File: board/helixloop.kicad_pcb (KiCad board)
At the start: 2 copper layers, 137.5 x 137.5 mm, 372 parts, among them J1 Conn_01x04, J2 Conn_01x02

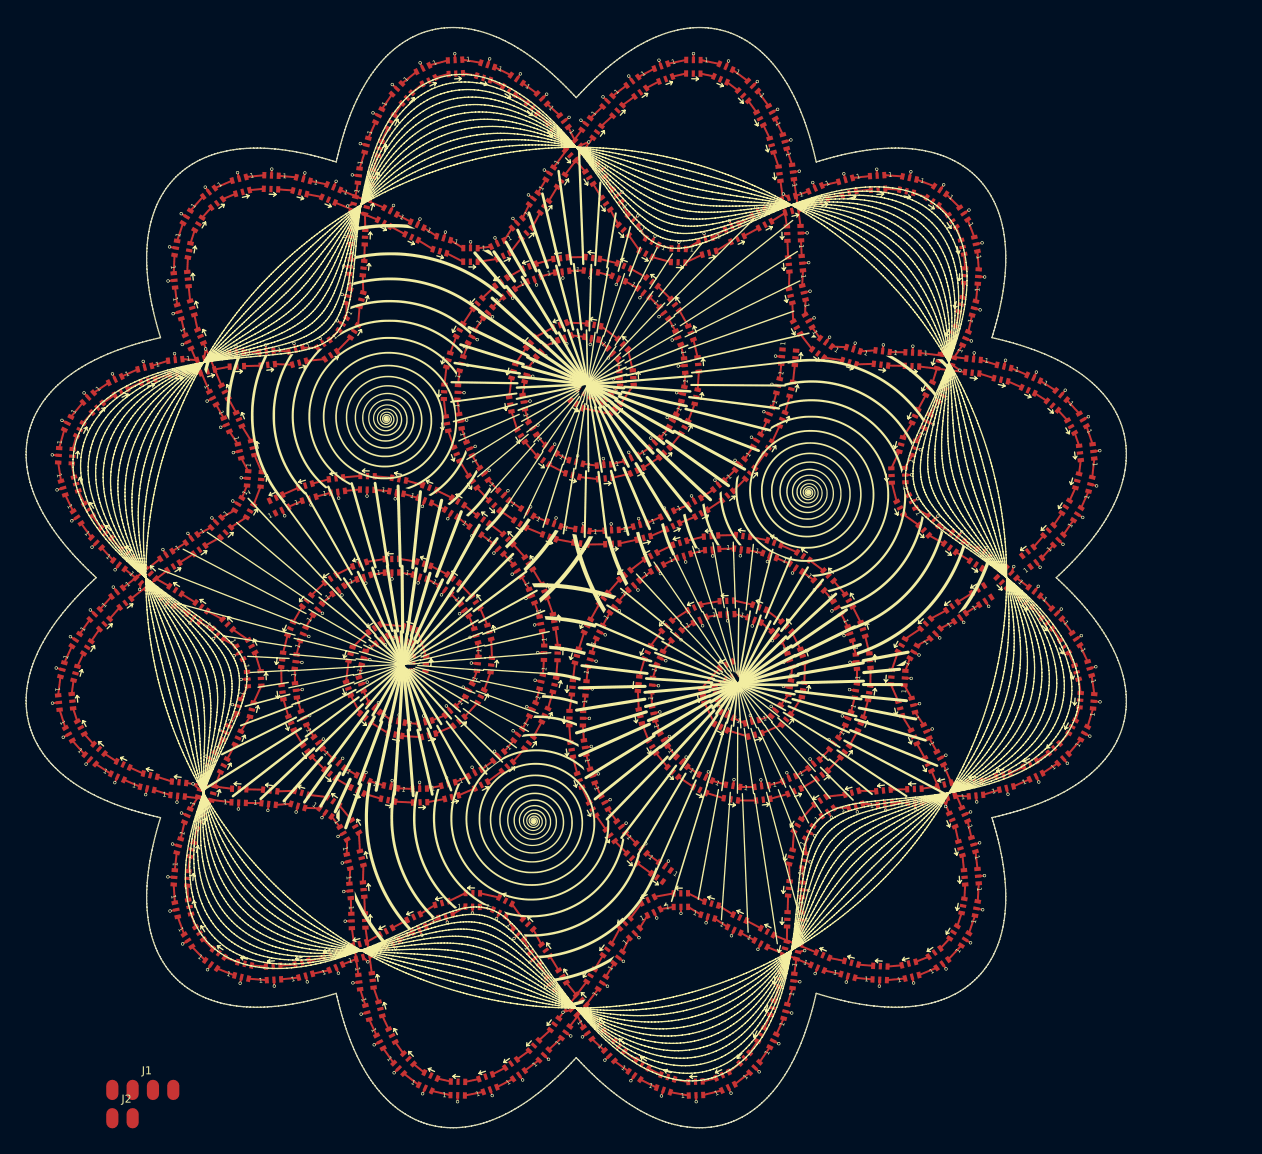
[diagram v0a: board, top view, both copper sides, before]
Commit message: refine the edge.cuts to be nice and smooth
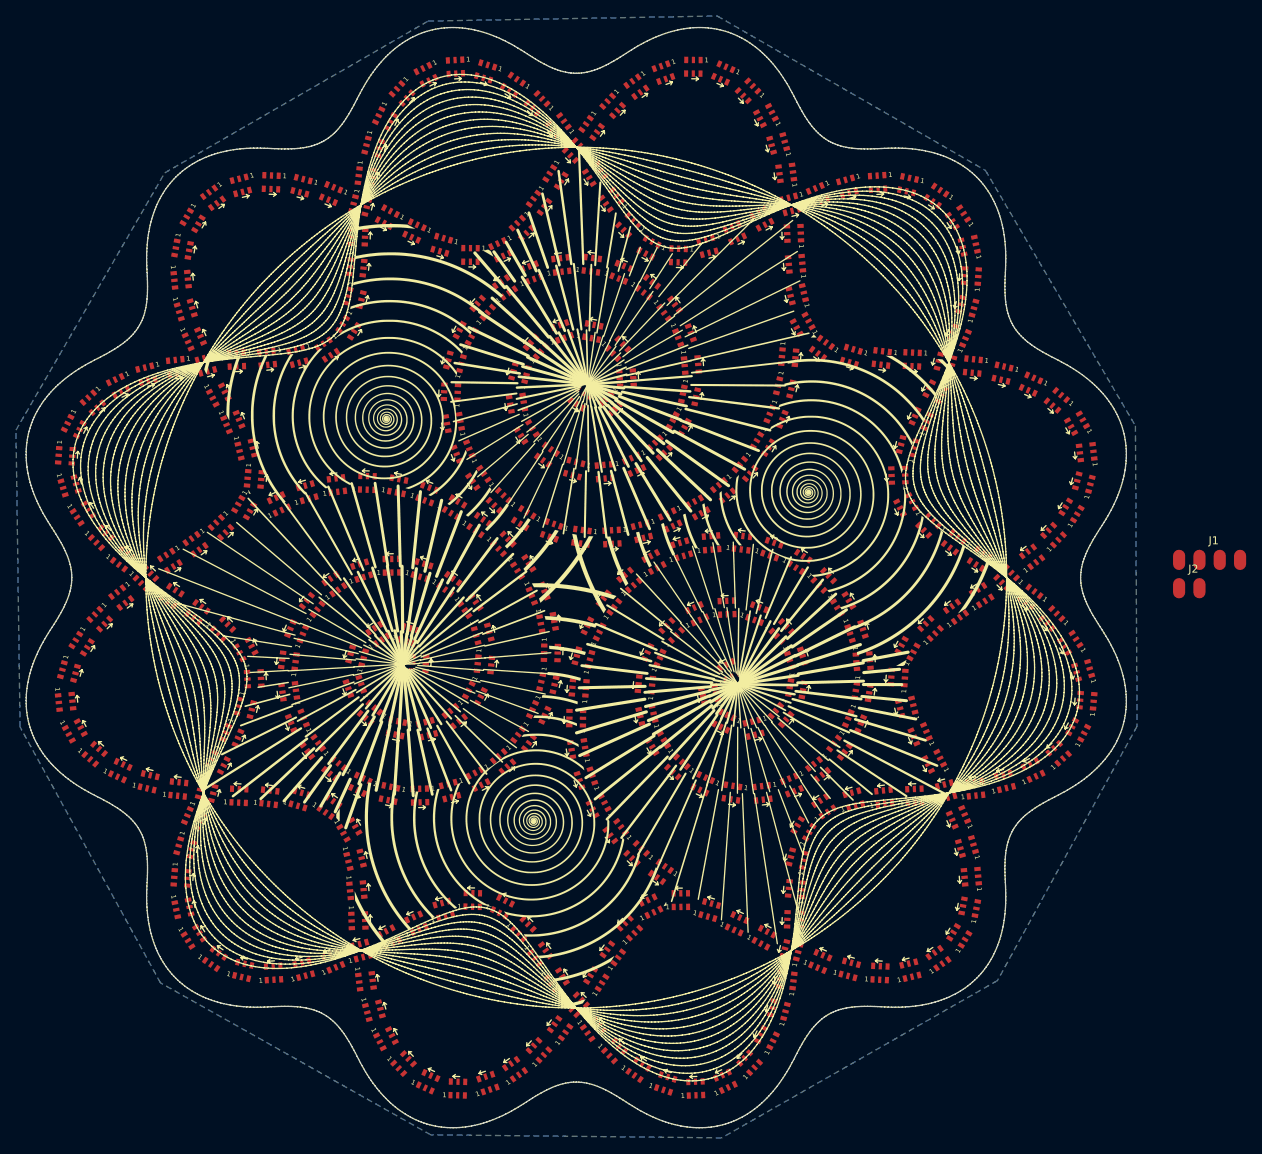
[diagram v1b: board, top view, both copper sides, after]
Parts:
- D1, D10, D100, D101, D102, D103, D104, D105, D106, D107, D108, D109, D11, D110, D111, D112, D113, D114, D115, D116, D117, D118, D119, D12, D120, D121, D122, D123, D124, D125, D126, D127, D128, D129, D13, D130, D131, D132, D133, D134, D135, D136, D137, D138, D139, D14, D140, D141, D142, D143, D144, D145, D146, D147, D148, D149, D15, D150, D151, D152, D153, D154, D155, D156, D157, D158, D159, D16, D160, D161, D162, D163, D164, D165, D166, D167, D168, D169, D17, D170, D171, D172, D173, D174, D175, D176, D177, D178, D179, D18, D180, D181, D182, D183, D184, D185, D186, D187, D188, D189, D19, D190, D191, D192, D193, D194, D195, D196, D197, D198, D199, D2, D20, D200, D201, D202, D203, D204, D205, D206, D207, D208, D209, D21, D210, D211, D212, D213, D214, D215, D216, D217, D218, D219, D22, D220, D221, D222, D223, D224, D225, D226, D227, D228, D229, D23, D230, D231, D232, D233, D234, D235, D236, D237, D238, D239, D24, D240, D241, D242, D243, D244, D245, D246, D247, D248, D249, D25, D250, D251, D252, D253, D254, D255, D256, D257, D258, D259, D26, D260, D261, D262, D263, D264, D265, D266, D267, D268, D269, D27, D270, D271, D272, D273, D274, D275, D276, D277, D278, D279, D28, D280, D281, D282, D283, D284, D285, D286, D287, D288, D289, D29, D290, D291, D292, D293, D294, D295, D296, D297, D298, D299, D3, D30, D300, D301, D302, D303, D304, D305, D306, D307, D308, D309, D31, D310, D311, D312, D313, D314, D315, D316, D317, D318, D319, D32, D320, D321, D322, D323, D324, D325, D326, D327, D328, D329, D33, D330, D331, D332, D333, D334, D335, D336, D337, D338, D339, D34, D340, D341, D342, D343, D344, D345, D346, D347, D348, D349, D35, D350, D351, D352, D353, D354, D355, D356, D357, D358, D359, D36, D360, D361, D362, D363, D364, D365, D366, D367, D368, D369, D37, D38, D39, D4, D40, D41, D42, D43, D44, D45, D46, D47, D48, D49, D5, D50, D51, D52, D53, D54, D55, D56, D57, D58, D59, D6, D60, D61, D62, D63, D64, D65, D66, D67, D68, D69, D7, D70, D71, D72, D73, D74, D75, D76, D77, D78, D79, D8, D80, D81, D82, D83, D84, D85, D86, D87, D88, D89, D9, D90, D91, D92, D93, D94, D95, D96, D97, D98, D99: value SK9822-EC20 -> LED-SK9822-EC20
- spiraldrawing: moved to F.SilkS
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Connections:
- D1 pad 1: Net-(D1-Pad1) -> (no net)
- D1 pad 2: GND -> (no net)
- D1 pad 3: /LED_SDI1 -> (no net)
- D1 pad 4: /LED_CKI1 -> (no net)
- D1 pad 5: +5V -> (no net)
- D1 pad 6: Net-(D1-Pad6) -> (no net)
- D10 pad 1: Net-(D10-Pad1) -> (no net)
- D10 pad 2: GND -> (no net)
- D10 pad 3: Net-(D10-Pad3) -> (no net)
- D10 pad 4: Net-(D10-Pad4) -> (no net)
- D10 pad 5: +5V -> (no net)
- D10 pad 6: Net-(D10-Pad6) -> (no net)
- D100 pad 1: Net-(D100-Pad1) -> (no net)
- D100 pad 2: GND -> (no net)
- D100 pad 3: Net-(D100-Pad3) -> (no net)
- D100 pad 4: Net-(D100-Pad4) -> (no net)
- D100 pad 5: +5V -> (no net)
- D100 pad 6: Net-(D100-Pad6) -> (no net)
- D101 pad 1: Net-(D101-Pad1) -> (no net)
- D101 pad 2: GND -> (no net)
- D101 pad 3: Net-(D100-Pad1) -> (no net)
- D101 pad 4: Net-(D100-Pad6) -> (no net)
- D101 pad 5: +5V -> (no net)
- D101 pad 6: Net-(D101-Pad6) -> (no net)
- D102 pad 1: Net-(D102-Pad1) -> (no net)
- D102 pad 2: GND -> (no net)
- D102 pad 3: Net-(D101-Pad1) -> (no net)
- D102 pad 4: Net-(D101-Pad6) -> (no net)
- D102 pad 5: +5V -> (no net)
- D102 pad 6: Net-(D102-Pad6) -> (no net)
- D103 pad 1: Net-(D103-Pad1) -> (no net)
- D103 pad 2: GND -> (no net)
- D103 pad 3: Net-(D102-Pad1) -> (no net)
- D103 pad 4: Net-(D102-Pad6) -> (no net)
- D103 pad 5: +5V -> (no net)
- D103 pad 6: Net-(D103-Pad6) -> (no net)
- D104 pad 1: Net-(D104-Pad1) -> (no net)
- D104 pad 2: GND -> (no net)
- D104 pad 3: Net-(D103-Pad1) -> (no net)
- D104 pad 4: Net-(D103-Pad6) -> (no net)
- D104 pad 5: +5V -> (no net)
- D104 pad 6: Net-(D104-Pad6) -> (no net)
- D105 pad 1: Net-(D105-Pad1) -> (no net)
- D105 pad 2: GND -> (no net)
- D105 pad 3: Net-(D104-Pad1) -> (no net)
- D105 pad 4: Net-(D104-Pad6) -> (no net)
- D105 pad 5: +5V -> (no net)
- D105 pad 6: Net-(D105-Pad6) -> (no net)
- D106 pad 1: Net-(D106-Pad1) -> (no net)
- D106 pad 2: GND -> (no net)
- D106 pad 3: Net-(D105-Pad1) -> (no net)
- D106 pad 4: Net-(D105-Pad6) -> (no net)
- D106 pad 5: +5V -> (no net)
- D106 pad 6: Net-(D106-Pad6) -> (no net)
- D107 pad 1: Net-(D107-Pad1) -> (no net)
- D107 pad 2: GND -> (no net)
- D107 pad 3: Net-(D106-Pad1) -> (no net)
- D107 pad 4: Net-(D106-Pad6) -> (no net)
- D107 pad 5: +5V -> (no net)
- D107 pad 6: Net-(D107-Pad6) -> (no net)
- D108 pad 1: Net-(D108-Pad1) -> (no net)
- D108 pad 2: GND -> (no net)
- D108 pad 3: Net-(D107-Pad1) -> (no net)
- D108 pad 4: Net-(D107-Pad6) -> (no net)
- D108 pad 5: +5V -> (no net)
- D108 pad 6: Net-(D108-Pad6) -> (no net)
- D109 pad 1: Net-(D109-Pad1) -> (no net)
- D109 pad 2: GND -> (no net)
- D109 pad 3: Net-(D108-Pad1) -> (no net)
- D109 pad 4: Net-(D108-Pad6) -> (no net)
- D109 pad 5: +5V -> (no net)
- D109 pad 6: Net-(D109-Pad6) -> (no net)
- D11 pad 1: Net-(D11-Pad1) -> (no net)
- D11 pad 2: GND -> (no net)
- D11 pad 3: Net-(D10-Pad1) -> (no net)
- D11 pad 4: Net-(D10-Pad6) -> (no net)
- D11 pad 5: +5V -> (no net)
- D11 pad 6: Net-(D11-Pad6) -> (no net)
- D110 pad 1: Net-(D110-Pad1) -> (no net)
- D110 pad 2: GND -> (no net)
- D110 pad 3: Net-(D109-Pad1) -> (no net)
- D110 pad 4: Net-(D109-Pad6) -> (no net)
- D110 pad 5: +5V -> (no net)
- D110 pad 6: Net-(D110-Pad6) -> (no net)
- D111 pad 1: Net-(D111-Pad1) -> (no net)
- D111 pad 2: GND -> (no net)
- D111 pad 3: Net-(D110-Pad1) -> (no net)
- D111 pad 4: Net-(D110-Pad6) -> (no net)
- D111 pad 5: +5V -> (no net)
- D111 pad 6: Net-(D111-Pad6) -> (no net)
- D112 pad 1: Net-(D112-Pad1) -> (no net)
- D112 pad 2: GND -> (no net)
- D112 pad 3: Net-(D111-Pad1) -> (no net)
- D112 pad 4: Net-(D111-Pad6) -> (no net)
- D112 pad 5: +5V -> (no net)
- D112 pad 6: Net-(D112-Pad6) -> (no net)
- D113 pad 1: Net-(D113-Pad1) -> (no net)
- D113 pad 2: GND -> (no net)
- D113 pad 3: Net-(D112-Pad1) -> (no net)
- D113 pad 4: Net-(D112-Pad6) -> (no net)
- D113 pad 5: +5V -> (no net)
- D113 pad 6: Net-(D113-Pad6) -> (no net)
- D114 pad 1: Net-(D114-Pad1) -> (no net)
- D114 pad 2: GND -> (no net)
- D114 pad 3: Net-(D113-Pad1) -> (no net)
- D114 pad 4: Net-(D113-Pad6) -> (no net)
- D114 pad 5: +5V -> (no net)
- D114 pad 6: Net-(D114-Pad6) -> (no net)
- D115 pad 1: Net-(D115-Pad1) -> (no net)
- D115 pad 2: GND -> (no net)
- D115 pad 3: Net-(D114-Pad1) -> (no net)
- D115 pad 4: Net-(D114-Pad6) -> (no net)
- D115 pad 5: +5V -> (no net)
- D115 pad 6: Net-(D115-Pad6) -> (no net)
- D116 pad 1: Net-(D116-Pad1) -> (no net)
- D116 pad 2: GND -> (no net)
- D116 pad 3: Net-(D115-Pad1) -> (no net)
- D116 pad 4: Net-(D115-Pad6) -> (no net)
- D116 pad 5: +5V -> (no net)
- D116 pad 6: Net-(D116-Pad6) -> (no net)
- D117 pad 1: Net-(D117-Pad1) -> (no net)
- D117 pad 2: GND -> (no net)
- D117 pad 3: Net-(D116-Pad1) -> (no net)
- D117 pad 4: Net-(D116-Pad6) -> (no net)
- D117 pad 5: +5V -> (no net)
- D117 pad 6: Net-(D117-Pad6) -> (no net)
- D118 pad 1: Net-(D118-Pad1) -> (no net)
- D118 pad 2: GND -> (no net)
- D118 pad 3: Net-(D117-Pad1) -> (no net)
- D118 pad 4: Net-(D117-Pad6) -> (no net)
- D118 pad 5: +5V -> (no net)
- D118 pad 6: Net-(D118-Pad6) -> (no net)
- D119 pad 1: Net-(D119-Pad1) -> (no net)
- D119 pad 2: GND -> (no net)
- D119 pad 3: Net-(D118-Pad1) -> (no net)
- D119 pad 4: Net-(D118-Pad6) -> (no net)
- D119 pad 5: +5V -> (no net)
- D119 pad 6: Net-(D119-Pad6) -> (no net)
- D12 pad 1: Net-(D12-Pad1) -> (no net)
- D12 pad 2: GND -> (no net)
- D12 pad 3: Net-(D11-Pad1) -> (no net)
- D12 pad 4: Net-(D11-Pad6) -> (no net)
- D12 pad 5: +5V -> (no net)
- D12 pad 6: Net-(D12-Pad6) -> (no net)
- D120 pad 1: Net-(D120-Pad1) -> (no net)
- D120 pad 2: GND -> (no net)
- D120 pad 3: Net-(D119-Pad1) -> (no net)
- D120 pad 4: Net-(D119-Pad6) -> (no net)
- D120 pad 5: +5V -> (no net)
- D120 pad 6: Net-(D120-Pad6) -> (no net)
- D121 pad 1: Net-(D121-Pad1) -> (no net)
- D121 pad 2: GND -> (no net)
- D121 pad 3: Net-(D120-Pad1) -> (no net)
- D121 pad 4: Net-(D120-Pad6) -> (no net)
- D121 pad 5: +5V -> (no net)
- D121 pad 6: Net-(D121-Pad6) -> (no net)
- D122 pad 1: Net-(D122-Pad1) -> (no net)
- D122 pad 2: GND -> (no net)
- D122 pad 3: Net-(D121-Pad1) -> (no net)
- D122 pad 4: Net-(D121-Pad6) -> (no net)
- D122 pad 5: +5V -> (no net)
- D122 pad 6: Net-(D122-Pad6) -> (no net)
- D123 pad 1: /SK9822 LED Array 1/LED_SDO -> (no net)
- D123 pad 2: GND -> (no net)
- D123 pad 3: Net-(D122-Pad1) -> (no net)
- D123 pad 4: Net-(D122-Pad6) -> (no net)
- D123 pad 5: +5V -> (no net)
- D123 pad 6: /SK9822 LED Array 1/LED_CKO -> (no net)
- D124 pad 1: Net-(D124-Pad1) -> (no net)
- D124 pad 2: GND -> (no net)
- D124 pad 3: /SK9822 LED Array 1/LED_SDO -> (no net)
- D124 pad 4: /SK9822 LED Array 1/LED_CKO -> (no net)
- D124 pad 5: +5V -> (no net)
- D124 pad 6: Net-(D124-Pad6) -> (no net)
- D125 pad 1: Net-(D125-Pad1) -> (no net)
- D125 pad 2: GND -> (no net)
- D125 pad 3: Net-(D124-Pad1) -> (no net)
- D125 pad 4: Net-(D124-Pad6) -> (no net)
- D125 pad 5: +5V -> (no net)
- D125 pad 6: Net-(D125-Pad6) -> (no net)
- D126 pad 1: Net-(D126-Pad1) -> (no net)
- D126 pad 2: GND -> (no net)
- D126 pad 3: Net-(D125-Pad1) -> (no net)
- D126 pad 4: Net-(D125-Pad6) -> (no net)
- D126 pad 5: +5V -> (no net)
- D126 pad 6: Net-(D126-Pad6) -> (no net)
- D127 pad 1: Net-(D127-Pad1) -> (no net)
- D127 pad 2: GND -> (no net)
- D127 pad 3: Net-(D126-Pad1) -> (no net)
- D127 pad 4: Net-(D126-Pad6) -> (no net)
- D127 pad 5: +5V -> (no net)
- D127 pad 6: Net-(D127-Pad6) -> (no net)
- D128 pad 1: Net-(D128-Pad1) -> (no net)
- D128 pad 2: GND -> (no net)
- D128 pad 3: Net-(D127-Pad1) -> (no net)
- D128 pad 4: Net-(D127-Pad6) -> (no net)
- D128 pad 5: +5V -> (no net)
- D128 pad 6: Net-(D128-Pad6) -> (no net)
- D129 pad 1: Net-(D129-Pad1) -> (no net)
- D129 pad 2: GND -> (no net)
- D129 pad 3: Net-(D128-Pad1) -> (no net)
- D129 pad 4: Net-(D128-Pad6) -> (no net)
- D129 pad 5: +5V -> (no net)
- D129 pad 6: Net-(D129-Pad6) -> (no net)
- D13 pad 1: Net-(D13-Pad1) -> (no net)
- D13 pad 2: GND -> (no net)
- D13 pad 3: Net-(D12-Pad1) -> (no net)
- D13 pad 4: Net-(D12-Pad6) -> (no net)
- D13 pad 5: +5V -> (no net)
- D13 pad 6: Net-(D13-Pad6) -> (no net)
- D130 pad 1: Net-(D130-Pad1) -> (no net)
- D130 pad 2: GND -> (no net)
- D130 pad 3: Net-(D129-Pad1) -> (no net)
- D130 pad 4: Net-(D129-Pad6) -> (no net)
- D130 pad 5: +5V -> (no net)
- D130 pad 6: Net-(D130-Pad6) -> (no net)
- D131 pad 1: Net-(D131-Pad1) -> (no net)
- D131 pad 2: GND -> (no net)
- D131 pad 3: Net-(D130-Pad1) -> (no net)
- D131 pad 4: Net-(D130-Pad6) -> (no net)
- D131 pad 5: +5V -> (no net)
- D131 pad 6: Net-(D131-Pad6) -> (no net)
- D132 pad 1: Net-(D132-Pad1) -> (no net)
- D132 pad 2: GND -> (no net)
- D132 pad 3: Net-(D131-Pad1) -> (no net)
- D132 pad 4: Net-(D131-Pad6) -> (no net)
- D132 pad 5: +5V -> (no net)
- D132 pad 6: Net-(D132-Pad6) -> (no net)
- D133 pad 1: Net-(D133-Pad1) -> (no net)
- D133 pad 2: GND -> (no net)
- D133 pad 3: Net-(D132-Pad1) -> (no net)
- D133 pad 4: Net-(D132-Pad6) -> (no net)
- D133 pad 5: +5V -> (no net)
- D133 pad 6: Net-(D133-Pad6) -> (no net)
- D134 pad 1: Net-(D134-Pad1) -> (no net)
- D134 pad 2: GND -> (no net)
- D134 pad 3: Net-(D133-Pad1) -> (no net)
- D134 pad 4: Net-(D133-Pad6) -> (no net)
- D134 pad 5: +5V -> (no net)
- D134 pad 6: Net-(D134-Pad6) -> (no net)
- D135 pad 1: Net-(D135-Pad1) -> (no net)
- D135 pad 2: GND -> (no net)
- D135 pad 3: Net-(D134-Pad1) -> (no net)
- D135 pad 4: Net-(D134-Pad6) -> (no net)
- D135 pad 5: +5V -> (no net)
- D135 pad 6: Net-(D135-Pad6) -> (no net)
- D136 pad 1: Net-(D136-Pad1) -> (no net)
- D136 pad 2: GND -> (no net)
- D136 pad 3: Net-(D135-Pad1) -> (no net)
- D136 pad 4: Net-(D135-Pad6) -> (no net)
- D136 pad 5: +5V -> (no net)
- D136 pad 6: Net-(D136-Pad6) -> (no net)
- D137 pad 1: Net-(D137-Pad1) -> (no net)
- D137 pad 2: GND -> (no net)
- D137 pad 3: Net-(D136-Pad1) -> (no net)
- D137 pad 4: Net-(D136-Pad6) -> (no net)
- D137 pad 5: +5V -> (no net)
- D137 pad 6: Net-(D137-Pad6) -> (no net)
- D138 pad 1: Net-(D139-Pad3) -> (no net)
- D138 pad 2: GND -> (no net)
- D138 pad 3: Net-(D137-Pad1) -> (no net)
- D138 pad 4: Net-(D137-Pad6) -> (no net)
- D138 pad 5: +5V -> (no net)
- D138 pad 6: Net-(D139-Pad4) -> (no net)
- D139 pad 1: Net-(D139-Pad1) -> (no net)
- D139 pad 2: GND -> (no net)
- D139 pad 3: Net-(D139-Pad3) -> (no net)
- D139 pad 4: Net-(D139-Pad4) -> (no net)
- D139 pad 5: +5V -> (no net)
- D139 pad 6: Net-(D139-Pad6) -> (no net)
- D14 pad 1: Net-(D14-Pad1) -> (no net)
- D14 pad 2: GND -> (no net)
- D14 pad 3: Net-(D13-Pad1) -> (no net)
- D14 pad 4: Net-(D13-Pad6) -> (no net)
- D14 pad 5: +5V -> (no net)
- D14 pad 6: Net-(D14-Pad6) -> (no net)
- D140 pad 1: Net-(D140-Pad1) -> (no net)
- D140 pad 2: GND -> (no net)
- D140 pad 3: Net-(D139-Pad1) -> (no net)
- D140 pad 4: Net-(D139-Pad6) -> (no net)
- D140 pad 5: +5V -> (no net)
- D140 pad 6: Net-(D140-Pad6) -> (no net)
- D141 pad 1: Net-(D141-Pad1) -> (no net)
- D141 pad 2: GND -> (no net)
- D141 pad 3: Net-(D140-Pad1) -> (no net)
- D141 pad 4: Net-(D140-Pad6) -> (no net)
- D141 pad 5: +5V -> (no net)
- D141 pad 6: Net-(D141-Pad6) -> (no net)
- D142 pad 1: Net-(D142-Pad1) -> (no net)
- D142 pad 2: GND -> (no net)
- D142 pad 3: Net-(D141-Pad1) -> (no net)
- D142 pad 4: Net-(D141-Pad6) -> (no net)
- D142 pad 5: +5V -> (no net)
- D142 pad 6: Net-(D142-Pad6) -> (no net)
- D143 pad 1: Net-(D143-Pad1) -> (no net)
- D143 pad 2: GND -> (no net)
- D143 pad 3: Net-(D142-Pad1) -> (no net)
- D143 pad 4: Net-(D142-Pad6) -> (no net)
- D143 pad 5: +5V -> (no net)
- D143 pad 6: Net-(D143-Pad6) -> (no net)
- D144 pad 1: Net-(D144-Pad1) -> (no net)
- D144 pad 2: GND -> (no net)
- D144 pad 3: Net-(D143-Pad1) -> (no net)
- D144 pad 4: Net-(D143-Pad6) -> (no net)
- D144 pad 5: +5V -> (no net)
- D144 pad 6: Net-(D144-Pad6) -> (no net)
- D145 pad 1: Net-(D145-Pad1) -> (no net)
- D145 pad 2: GND -> (no net)
- D145 pad 3: Net-(D144-Pad1) -> (no net)
- D145 pad 4: Net-(D144-Pad6) -> (no net)
- D145 pad 5: +5V -> (no net)
- D145 pad 6: Net-(D145-Pad6) -> (no net)
- D146 pad 1: Net-(D146-Pad1) -> (no net)
- D146 pad 2: GND -> (no net)
- D146 pad 3: Net-(D145-Pad1) -> (no net)
- D146 pad 4: Net-(D145-Pad6) -> (no net)
- D146 pad 5: +5V -> (no net)
- D146 pad 6: Net-(D146-Pad6) -> (no net)
- D147 pad 1: Net-(D147-Pad1) -> (no net)
- D147 pad 2: GND -> (no net)
- D147 pad 3: Net-(D146-Pad1) -> (no net)
- D147 pad 4: Net-(D146-Pad6) -> (no net)
- D147 pad 5: +5V -> (no net)
- D147 pad 6: Net-(D147-Pad6) -> (no net)
- D148 pad 1: Net-(D148-Pad1) -> (no net)
- D148 pad 2: GND -> (no net)
- D148 pad 3: Net-(D147-Pad1) -> (no net)
- D148 pad 4: Net-(D147-Pad6) -> (no net)
- D148 pad 5: +5V -> (no net)
- D148 pad 6: Net-(D148-Pad6) -> (no net)
- D149 pad 1: Net-(D149-Pad1) -> (no net)
- D149 pad 2: GND -> (no net)
- D149 pad 3: Net-(D148-Pad1) -> (no net)
- D149 pad 4: Net-(D148-Pad6) -> (no net)
- D149 pad 5: +5V -> (no net)
- D149 pad 6: Net-(D149-Pad6) -> (no net)
- D15 pad 1: Net-(D16-Pad3) -> (no net)
- D15 pad 2: GND -> (no net)
- D15 pad 3: Net-(D14-Pad1) -> (no net)
- D15 pad 4: Net-(D14-Pad6) -> (no net)
- D15 pad 5: +5V -> (no net)
- D15 pad 6: Net-(D16-Pad4) -> (no net)
- D150 pad 1: Net-(D150-Pad1) -> (no net)
- D150 pad 2: GND -> (no net)
- D150 pad 3: Net-(D149-Pad1) -> (no net)
- D150 pad 4: Net-(D149-Pad6) -> (no net)
- D150 pad 5: +5V -> (no net)
- D150 pad 6: Net-(D150-Pad6) -> (no net)
- D151 pad 1: Net-(D151-Pad1) -> (no net)
- D151 pad 2: GND -> (no net)
- D151 pad 3: Net-(D150-Pad1) -> (no net)
- D151 pad 4: Net-(D150-Pad6) -> (no net)
- D151 pad 5: +5V -> (no net)
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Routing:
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- added copper zone on B.Cu, net GND
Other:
- outline, holes or cut-outs redrawn

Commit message: finally get pixels all aligned right by laying out the sine-wave in chunks and using different pixel spacing for outer vs inner curve
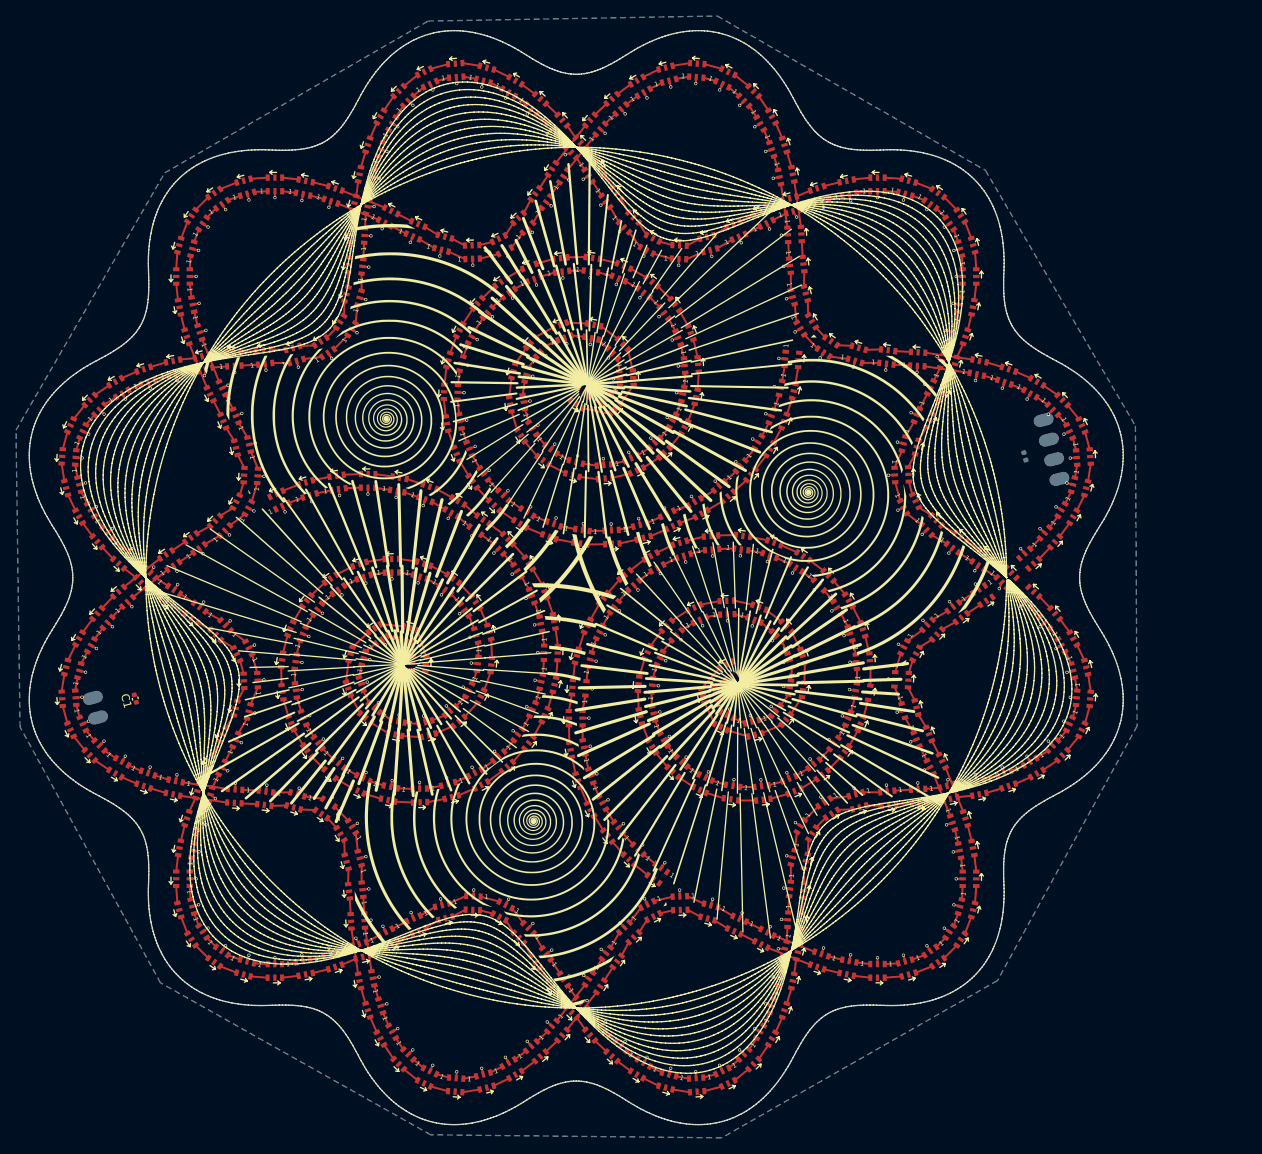
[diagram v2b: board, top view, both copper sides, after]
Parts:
- added C1: 10uF, Capacitor_SMD:C_0402_1005Metric, F.Cu at (44.9, 115.1)
- added C2: 10uF, Capacitor_SMD:C_0402_1005Metric, B.Cu at (156.1, 84.8)
- J1, J2: moved to B.Cu
- spiraldrawing: moved to F.Cu
- moved J2 137.4 mm to (40.0, 116.2), turned to -75 degrees
- moved D148 115.9 mm to (102.4, 43.4), turned to -131.363 degrees
- moved D202 115.8 mm to (97.6, 156.6), turned to 48.6371 degrees
- moved D147 115.7 mm to (105.0, 40.8), turned to -138.828 degrees
- moved D201 115.6 mm to (95.0, 159.2), turned to 41.1715 degrees
- moved D91 113.3 mm to (102.4, 156.6), turned to -48.6561 degrees
- moved D31 113.1 mm to (97.6, 43.4), turned to 131.344 degrees
- moved D90 113.1 mm to (100.0, 153.7), turned to -44.9689 degrees
- moved D30 113.0 mm to (100.0, 46.3), turned to 135.031 degrees
- moved D92 112.7 mm to (105.0, 159.2), turned to -41.201 degrees
- moved D32 112.7 mm to (95.0, 40.8), turned to 138.799 degrees
- moved D89 112.5 mm to (97.7, 150.7), turned to -56.7109 degrees
- moved D29 112.4 mm to (102.3, 49.3), turned to 123.289 degrees
- moved D149 112.2 mm to (97.7, 49.4), turned to -123.328 degrees
- moved D203 112.1 mm to (102.3, 150.6), turned to 56.6721 degrees
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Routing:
- net (no net): track 0.00 -> 1552.5 mm, vias 0 -> 14
- net GND: track 0.00 -> 282.4 mm, vias 0 -> 353
- net +5V: track 0.00 -> 1.60 mm, vias 0 -> 2
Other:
- board size 137.5 x 137.5 mm -> 136.7 x 136.7 mm

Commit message: draft routing
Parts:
- C1: moved to B.Cu
- D1, D10, D100, D101, D102, D103, D104, D105, D106, D107, D108, D109, D11, D110, D111, D112, D113, D114, D115, D116, D117, D118, D119, D12, D120, D121, D122, D123, D124, D125, D126, D127, D128, D129, D13, D130, D131, D132, D133, D134, D135, D136, D137, D138, D139, D14, D140, D141, D142, D143, D144, D145, D146, D147, D148, D149, D15, D150, D151, D152, D153, D154, D155, D156, D157, D158, D159, D16, D160, D161, D162, D163, D164, D165, D166, D167, D168, D169, D17, D170, D171, D172, D173, D174, D175, D176, D177, D178, D179, D18, D180, D181, D182, D183, D184, D185, D186, D187, D188, D189, D19, D190, D191, D192, D193, D194, D195, D196, D197, D198, D199, D2, D20, D200, D201, D202, D203, D204, D205, D206, D207, D208, D209, D21, D210, D211, D212, D213, D214, D215, D216, D217, D218, D219, D22, D220, D221, D222, D223, D224, D225, D226, D227, D228, D229, D23, D230, D231, D232, D233, D234, D235, D236, D237, D238, D239, D24, D240, D241, D242, D243, D244, D245, D246, D247, D248, D249, D25, D250, D251, D252, D253, D254, D255, D256, D257, D258, D259, D26, D260, D261, D262, D263, D264, D265, D266, D267, D268, D269, D27, D270, D271, D272, D273, D274, D275, D276, D277, D278, D279, D28, D280, D281, D282, D283, D284, D285, D286, D287, D288, D289, D29, D290, D291, D292, D293, D294, D295, D296, D297, D298, D299, D3, D30, D300, D301, D302, D303, D304, D305, D306, D307, D308, D309, D31, D310, D311, D312, D313, D314, D315, D316, D317, D318, D319, D32, D320, D321, D322, D323, D324, D325, D326, D327, D328, D329, D33, D330, D331, D332, D333, D334, D335, D336, D337, D338, D339, D34, D340, D341, D342, D343, D344, D345, D346, D347, D348, D349, D35, D350, D351, D352, D353, D354, D355, D356, D357, D358, D359, D36, D360, D361, D362, D363, D364, D365, D366, D367, D368, D369, D37, D38, D39, D4, D40, D41, D42, D43, D44, D45, D46, D47, D48, D49, D5, D50, D51, D52, D53, D54, D55, D56, D57, D58, D59, D6, D60, D61, D62, D63, D64, D65, D66, D67, D68, D69, D7, D70, D71, D72, D73, D74, D75, D76, D77, D78, D79, D8, D80, D81, D82, D83, D84, D85, D86, D87, D88, D89, D9, D90, D91, D92, D93, D94, D95, D96, D97, D98, D99: value LED-SK9822-EC20 -> SK9822-EC20
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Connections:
- D1 pad 1: (no net) -> Net-(D1-Pad1)
- D1 pad 2: (no net) -> GND
- D1 pad 3: (no net) -> /LED_SDI1
- D1 pad 4: (no net) -> /LED_CKI1
- D1 pad 5: (no net) -> +5V
- D1 pad 6: (no net) -> Net-(D1-Pad6)
- D10 pad 1: (no net) -> Net-(D10-Pad1)
- D10 pad 2: (no net) -> GND
- D10 pad 3: (no net) -> Net-(D10-Pad3)
- D10 pad 4: (no net) -> Net-(D10-Pad4)
- D10 pad 5: (no net) -> +5V
- D10 pad 6: (no net) -> Net-(D10-Pad6)
- D100 pad 1: (no net) -> Net-(D100-Pad1)
- D100 pad 2: (no net) -> GND
- D100 pad 3: (no net) -> Net-(D100-Pad3)
- D100 pad 4: (no net) -> Net-(D100-Pad4)
- D100 pad 5: (no net) -> +5V
- D100 pad 6: (no net) -> Net-(D100-Pad6)
- D101 pad 1: (no net) -> Net-(D101-Pad1)
- D101 pad 2: (no net) -> GND
- D101 pad 3: (no net) -> Net-(D100-Pad1)
- D101 pad 4: (no net) -> Net-(D100-Pad6)
- D101 pad 5: (no net) -> +5V
- D101 pad 6: (no net) -> Net-(D101-Pad6)
- D102 pad 1: (no net) -> Net-(D102-Pad1)
- D102 pad 2: (no net) -> GND
- D102 pad 3: (no net) -> Net-(D101-Pad1)
- D102 pad 4: (no net) -> Net-(D101-Pad6)
- D102 pad 5: (no net) -> +5V
- D102 pad 6: (no net) -> Net-(D102-Pad6)
- D103 pad 1: (no net) -> Net-(D103-Pad1)
- D103 pad 2: (no net) -> GND
- D103 pad 3: (no net) -> Net-(D102-Pad1)
- D103 pad 4: (no net) -> Net-(D102-Pad6)
- D103 pad 5: (no net) -> +5V
- D103 pad 6: (no net) -> Net-(D103-Pad6)
- D104 pad 1: (no net) -> Net-(D104-Pad1)
- D104 pad 2: (no net) -> GND
- D104 pad 3: (no net) -> Net-(D103-Pad1)
- D104 pad 4: (no net) -> Net-(D103-Pad6)
- D104 pad 5: (no net) -> +5V
- D104 pad 6: (no net) -> Net-(D104-Pad6)
- D105 pad 1: (no net) -> Net-(D105-Pad1)
- D105 pad 2: (no net) -> GND
- D105 pad 3: (no net) -> Net-(D104-Pad1)
- D105 pad 4: (no net) -> Net-(D104-Pad6)
- D105 pad 5: (no net) -> +5V
- D105 pad 6: (no net) -> Net-(D105-Pad6)
- D106 pad 1: (no net) -> Net-(D106-Pad1)
- D106 pad 2: (no net) -> GND
- D106 pad 3: (no net) -> Net-(D105-Pad1)
- D106 pad 4: (no net) -> Net-(D105-Pad6)
- D106 pad 5: (no net) -> +5V
- D106 pad 6: (no net) -> Net-(D106-Pad6)
- D107 pad 1: (no net) -> Net-(D107-Pad1)
- D107 pad 2: (no net) -> GND
- D107 pad 3: (no net) -> Net-(D106-Pad1)
- D107 pad 4: (no net) -> Net-(D106-Pad6)
- D107 pad 5: (no net) -> +5V
- D107 pad 6: (no net) -> Net-(D107-Pad6)
- D108 pad 1: (no net) -> Net-(D108-Pad1)
- D108 pad 2: (no net) -> GND
- D108 pad 3: (no net) -> Net-(D107-Pad1)
- D108 pad 4: (no net) -> Net-(D107-Pad6)
- D108 pad 5: (no net) -> +5V
- D108 pad 6: (no net) -> Net-(D108-Pad6)
- D109 pad 1: (no net) -> Net-(D109-Pad1)
- D109 pad 2: (no net) -> GND
- D109 pad 3: (no net) -> Net-(D108-Pad1)
- D109 pad 4: (no net) -> Net-(D108-Pad6)
- D109 pad 5: (no net) -> +5V
- D109 pad 6: (no net) -> Net-(D109-Pad6)
- D11 pad 1: (no net) -> Net-(D11-Pad1)
- D11 pad 2: (no net) -> GND
- D11 pad 3: (no net) -> Net-(D10-Pad1)
- D11 pad 4: (no net) -> Net-(D10-Pad6)
- D11 pad 5: (no net) -> +5V
- D11 pad 6: (no net) -> Net-(D11-Pad6)
- D110 pad 1: (no net) -> Net-(D110-Pad1)
- D110 pad 2: (no net) -> GND
- D110 pad 3: (no net) -> Net-(D109-Pad1)
- D110 pad 4: (no net) -> Net-(D109-Pad6)
- D110 pad 5: (no net) -> +5V
- D110 pad 6: (no net) -> Net-(D110-Pad6)
- D111 pad 1: (no net) -> Net-(D111-Pad1)
- D111 pad 2: (no net) -> GND
- D111 pad 3: (no net) -> Net-(D110-Pad1)
- D111 pad 4: (no net) -> Net-(D110-Pad6)
- D111 pad 5: (no net) -> +5V
- D111 pad 6: (no net) -> Net-(D111-Pad6)
- D112 pad 1: (no net) -> Net-(D112-Pad1)
- D112 pad 2: (no net) -> GND
- D112 pad 3: (no net) -> Net-(D111-Pad1)
- D112 pad 4: (no net) -> Net-(D111-Pad6)
- D112 pad 5: (no net) -> +5V
- D112 pad 6: (no net) -> Net-(D112-Pad6)
- D113 pad 1: (no net) -> Net-(D113-Pad1)
- D113 pad 2: (no net) -> GND
- D113 pad 3: (no net) -> Net-(D112-Pad1)
- D113 pad 4: (no net) -> Net-(D112-Pad6)
- D113 pad 5: (no net) -> +5V
- D113 pad 6: (no net) -> Net-(D113-Pad6)
- D114 pad 1: (no net) -> Net-(D114-Pad1)
- D114 pad 2: (no net) -> GND
- D114 pad 3: (no net) -> Net-(D113-Pad1)
- D114 pad 4: (no net) -> Net-(D113-Pad6)
- D114 pad 5: (no net) -> +5V
- D114 pad 6: (no net) -> Net-(D114-Pad6)
- D115 pad 1: (no net) -> Net-(D115-Pad1)
- D115 pad 2: (no net) -> GND
- D115 pad 3: (no net) -> Net-(D114-Pad1)
- D115 pad 4: (no net) -> Net-(D114-Pad6)
- D115 pad 5: (no net) -> +5V
- D115 pad 6: (no net) -> Net-(D115-Pad6)
- D116 pad 1: (no net) -> Net-(D116-Pad1)
- D116 pad 2: (no net) -> GND
- D116 pad 3: (no net) -> Net-(D115-Pad1)
- D116 pad 4: (no net) -> Net-(D115-Pad6)
- D116 pad 5: (no net) -> +5V
- D116 pad 6: (no net) -> Net-(D116-Pad6)
- D117 pad 1: (no net) -> Net-(D117-Pad1)
- D117 pad 2: (no net) -> GND
- D117 pad 3: (no net) -> Net-(D116-Pad1)
- D117 pad 4: (no net) -> Net-(D116-Pad6)
- D117 pad 5: (no net) -> +5V
- D117 pad 6: (no net) -> Net-(D117-Pad6)
- D118 pad 1: (no net) -> Net-(D118-Pad1)
- D118 pad 2: (no net) -> GND
- D118 pad 3: (no net) -> Net-(D117-Pad1)
- D118 pad 4: (no net) -> Net-(D117-Pad6)
- D118 pad 5: (no net) -> +5V
- D118 pad 6: (no net) -> Net-(D118-Pad6)
- D119 pad 1: (no net) -> Net-(D119-Pad1)
- D119 pad 2: (no net) -> GND
- D119 pad 3: (no net) -> Net-(D118-Pad1)
- D119 pad 4: (no net) -> Net-(D118-Pad6)
- D119 pad 5: (no net) -> +5V
- D119 pad 6: (no net) -> Net-(D119-Pad6)
- D12 pad 1: (no net) -> Net-(D12-Pad1)
- D12 pad 2: (no net) -> GND
- D12 pad 3: (no net) -> Net-(D11-Pad1)
- D12 pad 4: (no net) -> Net-(D11-Pad6)
- D12 pad 5: (no net) -> +5V
- D12 pad 6: (no net) -> Net-(D12-Pad6)
- D120 pad 1: (no net) -> Net-(D120-Pad1)
- D120 pad 2: (no net) -> GND
- D120 pad 3: (no net) -> Net-(D119-Pad1)
- D120 pad 4: (no net) -> Net-(D119-Pad6)
- D120 pad 5: (no net) -> +5V
- D120 pad 6: (no net) -> Net-(D120-Pad6)
- D121 pad 1: (no net) -> Net-(D121-Pad1)
- D121 pad 2: (no net) -> GND
- D121 pad 3: (no net) -> Net-(D120-Pad1)
- D121 pad 4: (no net) -> Net-(D120-Pad6)
- D121 pad 5: (no net) -> +5V
- D121 pad 6: (no net) -> Net-(D121-Pad6)
- D122 pad 1: (no net) -> Net-(D122-Pad1)
- D122 pad 2: (no net) -> GND
- D122 pad 3: (no net) -> Net-(D121-Pad1)
- D122 pad 4: (no net) -> Net-(D121-Pad6)
- D122 pad 5: (no net) -> +5V
- D122 pad 6: (no net) -> Net-(D122-Pad6)
- D123 pad 1: (no net) -> /SK9822 LED Array 1/LED_SDO
- D123 pad 2: (no net) -> GND
- D123 pad 3: (no net) -> Net-(D122-Pad1)
- D123 pad 4: (no net) -> Net-(D122-Pad6)
- D123 pad 5: (no net) -> +5V
- D123 pad 6: (no net) -> /SK9822 LED Array 1/LED_CKO
- D124 pad 1: (no net) -> Net-(D124-Pad1)
- D124 pad 2: (no net) -> GND
- D124 pad 3: (no net) -> /SK9822 LED Array 1/LED_SDO
- D124 pad 4: (no net) -> /SK9822 LED Array 1/LED_CKO
- D124 pad 5: (no net) -> +5V
- D124 pad 6: (no net) -> Net-(D124-Pad6)
- D125 pad 1: (no net) -> Net-(D125-Pad1)
- D125 pad 2: (no net) -> GND
- D125 pad 3: (no net) -> Net-(D124-Pad1)
- D125 pad 4: (no net) -> Net-(D124-Pad6)
- D125 pad 5: (no net) -> +5V
- D125 pad 6: (no net) -> Net-(D125-Pad6)
- D126 pad 1: (no net) -> Net-(D126-Pad1)
- D126 pad 2: (no net) -> GND
- D126 pad 3: (no net) -> Net-(D125-Pad1)
- D126 pad 4: (no net) -> Net-(D125-Pad6)
- D126 pad 5: (no net) -> +5V
- D126 pad 6: (no net) -> Net-(D126-Pad6)
- D127 pad 1: (no net) -> Net-(D127-Pad1)
- D127 pad 2: (no net) -> GND
- D127 pad 3: (no net) -> Net-(D126-Pad1)
- D127 pad 4: (no net) -> Net-(D126-Pad6)
- D127 pad 5: (no net) -> +5V
- D127 pad 6: (no net) -> Net-(D127-Pad6)
- D128 pad 1: (no net) -> Net-(D128-Pad1)
- D128 pad 2: (no net) -> GND
- D128 pad 3: (no net) -> Net-(D127-Pad1)
- D128 pad 4: (no net) -> Net-(D127-Pad6)
- D128 pad 5: (no net) -> +5V
- D128 pad 6: (no net) -> Net-(D128-Pad6)
- D129 pad 1: (no net) -> Net-(D129-Pad1)
- D129 pad 2: (no net) -> GND
- D129 pad 3: (no net) -> Net-(D128-Pad1)
- D129 pad 4: (no net) -> Net-(D128-Pad6)
- D129 pad 5: (no net) -> +5V
- D129 pad 6: (no net) -> Net-(D129-Pad6)
- D13 pad 1: (no net) -> Net-(D13-Pad1)
- D13 pad 2: (no net) -> GND
- D13 pad 3: (no net) -> Net-(D12-Pad1)
- D13 pad 4: (no net) -> Net-(D12-Pad6)
- D13 pad 5: (no net) -> +5V
- D13 pad 6: (no net) -> Net-(D13-Pad6)
- D130 pad 1: (no net) -> Net-(D130-Pad1)
- D130 pad 2: (no net) -> GND
- D130 pad 3: (no net) -> Net-(D129-Pad1)
- D130 pad 4: (no net) -> Net-(D129-Pad6)
- D130 pad 5: (no net) -> +5V
- D130 pad 6: (no net) -> Net-(D130-Pad6)
- D131 pad 1: (no net) -> Net-(D131-Pad1)
- D131 pad 2: (no net) -> GND
- D131 pad 3: (no net) -> Net-(D130-Pad1)
- D131 pad 4: (no net) -> Net-(D130-Pad6)
- D131 pad 5: (no net) -> +5V
- D131 pad 6: (no net) -> Net-(D131-Pad6)
- D132 pad 1: (no net) -> Net-(D132-Pad1)
- D132 pad 2: (no net) -> GND
- D132 pad 3: (no net) -> Net-(D131-Pad1)
- D132 pad 4: (no net) -> Net-(D131-Pad6)
- D132 pad 5: (no net) -> +5V
- D132 pad 6: (no net) -> Net-(D132-Pad6)
- D133 pad 1: (no net) -> Net-(D133-Pad1)
- D133 pad 2: (no net) -> GND
- D133 pad 3: (no net) -> Net-(D132-Pad1)
- D133 pad 4: (no net) -> Net-(D132-Pad6)
- D133 pad 5: (no net) -> +5V
- D133 pad 6: (no net) -> Net-(D133-Pad6)
- D134 pad 1: (no net) -> Net-(D134-Pad1)
- D134 pad 2: (no net) -> GND
- D134 pad 3: (no net) -> Net-(D133-Pad1)
- D134 pad 4: (no net) -> Net-(D133-Pad6)
- D134 pad 5: (no net) -> +5V
- D134 pad 6: (no net) -> Net-(D134-Pad6)
- D135 pad 1: (no net) -> Net-(D135-Pad1)
- D135 pad 2: (no net) -> GND
- D135 pad 3: (no net) -> Net-(D134-Pad1)
- D135 pad 4: (no net) -> Net-(D134-Pad6)
- D135 pad 5: (no net) -> +5V
- D135 pad 6: (no net) -> Net-(D135-Pad6)
- D136 pad 1: (no net) -> Net-(D136-Pad1)
- D136 pad 2: (no net) -> GND
- D136 pad 3: (no net) -> Net-(D135-Pad1)
- D136 pad 4: (no net) -> Net-(D135-Pad6)
- D136 pad 5: (no net) -> +5V
- D136 pad 6: (no net) -> Net-(D136-Pad6)
- D137 pad 1: (no net) -> Net-(D137-Pad1)
- D137 pad 2: (no net) -> GND
- D137 pad 3: (no net) -> Net-(D136-Pad1)
- D137 pad 4: (no net) -> Net-(D136-Pad6)
- D137 pad 5: (no net) -> +5V
- D137 pad 6: (no net) -> Net-(D137-Pad6)
- D138 pad 1: (no net) -> Net-(D139-Pad3)
- D138 pad 2: (no net) -> GND
- D138 pad 3: (no net) -> Net-(D137-Pad1)
- D138 pad 4: (no net) -> Net-(D137-Pad6)
- D138 pad 5: (no net) -> +5V
- D138 pad 6: (no net) -> Net-(D139-Pad4)
- D139 pad 1: (no net) -> Net-(D139-Pad1)
- D139 pad 2: (no net) -> GND
- D139 pad 3: (no net) -> Net-(D139-Pad3)
- D139 pad 4: (no net) -> Net-(D139-Pad4)
- D139 pad 5: (no net) -> +5V
- D139 pad 6: (no net) -> Net-(D139-Pad6)
- D14 pad 1: (no net) -> Net-(D14-Pad1)
- D14 pad 2: (no net) -> GND
- D14 pad 3: (no net) -> Net-(D13-Pad1)
- D14 pad 4: (no net) -> Net-(D13-Pad6)
- D14 pad 5: (no net) -> +5V
- D14 pad 6: (no net) -> Net-(D14-Pad6)
- D140 pad 1: (no net) -> Net-(D140-Pad1)
- D140 pad 2: (no net) -> GND
- D140 pad 3: (no net) -> Net-(D139-Pad1)
- D140 pad 4: (no net) -> Net-(D139-Pad6)
- D140 pad 5: (no net) -> +5V
- D140 pad 6: (no net) -> Net-(D140-Pad6)
- D141 pad 1: (no net) -> Net-(D141-Pad1)
- D141 pad 2: (no net) -> GND
- D141 pad 3: (no net) -> Net-(D140-Pad1)
- D141 pad 4: (no net) -> Net-(D140-Pad6)
- D141 pad 5: (no net) -> +5V
- D141 pad 6: (no net) -> Net-(D141-Pad6)
- D142 pad 1: (no net) -> Net-(D142-Pad1)
- D142 pad 2: (no net) -> GND
- D142 pad 3: (no net) -> Net-(D141-Pad1)
- D142 pad 4: (no net) -> Net-(D141-Pad6)
- D142 pad 5: (no net) -> +5V
- D142 pad 6: (no net) -> Net-(D142-Pad6)
- D143 pad 1: (no net) -> Net-(D143-Pad1)
- D143 pad 2: (no net) -> GND
- D143 pad 3: (no net) -> Net-(D142-Pad1)
- D143 pad 4: (no net) -> Net-(D142-Pad6)
- D143 pad 5: (no net) -> +5V
- D143 pad 6: (no net) -> Net-(D143-Pad6)
- D144 pad 1: (no net) -> Net-(D144-Pad1)
- D144 pad 2: (no net) -> GND
- D144 pad 3: (no net) -> Net-(D143-Pad1)
- D144 pad 4: (no net) -> Net-(D143-Pad6)
- D144 pad 5: (no net) -> +5V
- D144 pad 6: (no net) -> Net-(D144-Pad6)
- D145 pad 1: (no net) -> Net-(D145-Pad1)
- D145 pad 2: (no net) -> GND
- D145 pad 3: (no net) -> Net-(D144-Pad1)
- D145 pad 4: (no net) -> Net-(D144-Pad6)
- D145 pad 5: (no net) -> +5V
- D145 pad 6: (no net) -> Net-(D145-Pad6)
- D146 pad 1: (no net) -> Net-(D146-Pad1)
- D146 pad 2: (no net) -> GND
- D146 pad 3: (no net) -> Net-(D145-Pad1)
- D146 pad 4: (no net) -> Net-(D145-Pad6)
- D146 pad 5: (no net) -> +5V
- D146 pad 6: (no net) -> Net-(D146-Pad6)
- D147 pad 1: (no net) -> Net-(D147-Pad1)
- D147 pad 2: (no net) -> GND
- D147 pad 3: (no net) -> Net-(D146-Pad1)
- D147 pad 4: (no net) -> Net-(D146-Pad6)
- D147 pad 5: (no net) -> +5V
- D147 pad 6: (no net) -> Net-(D147-Pad6)
- D148 pad 1: (no net) -> Net-(D148-Pad1)
- D148 pad 2: (no net) -> GND
- D148 pad 3: (no net) -> Net-(D147-Pad1)
- D148 pad 4: (no net) -> Net-(D147-Pad6)
- D148 pad 5: (no net) -> +5V
- D148 pad 6: (no net) -> Net-(D148-Pad6)
- D149 pad 1: (no net) -> Net-(D149-Pad1)
- D149 pad 2: (no net) -> GND
- D149 pad 3: (no net) -> Net-(D148-Pad1)
- D149 pad 4: (no net) -> Net-(D148-Pad6)
- D149 pad 5: (no net) -> +5V
- D149 pad 6: (no net) -> Net-(D149-Pad6)
- D15 pad 1: (no net) -> Net-(D16-Pad3)
- D15 pad 2: (no net) -> GND
- D15 pad 3: (no net) -> Net-(D14-Pad1)
- D15 pad 4: (no net) -> Net-(D14-Pad6)
- D15 pad 5: (no net) -> +5V
- D15 pad 6: (no net) -> Net-(D16-Pad4)
- D150 pad 1: (no net) -> Net-(D150-Pad1)
- D150 pad 2: (no net) -> GND
- D150 pad 3: (no net) -> Net-(D149-Pad1)
- D150 pad 4: (no net) -> Net-(D149-Pad6)
- D150 pad 5: (no net) -> +5V
- D150 pad 6: (no net) -> Net-(D150-Pad6)
- D151 pad 1: (no net) -> Net-(D151-Pad1)
- D151 pad 2: (no net) -> GND
- D151 pad 3: (no net) -> Net-(D150-Pad1)
- D151 pad 4: (no net) -> Net-(D150-Pad6)
- D151 pad 5: (no net) -> +5V
- D151 pad 6: (no net) -> Net-(D151-Pad6)
- D152 pad 1: (no net) -> Net-(D152-Pad1)
- D152 pad 2: (no net) -> GND
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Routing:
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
